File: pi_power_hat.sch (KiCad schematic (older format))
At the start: 21 parts, among them J1 GPIO_CONNECTOR, J2 Barrel_Jack, J3 PIR Motion Sensor, J4 DH22T, J5 Screw_Terminal_01x02, Q1 DMG1012UW-7

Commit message: Add input connectors
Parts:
- J2: footprint (none) -> CON-SOCJ-2155:GRAVITECH_CON-SOCJ-2155; symbol Connector:Barrel_Jack -> Connector:Barrel_Jack_Switch
- J5: footprint (none) -> CONN-TH_P5.00_KF301-5.0-2P:CONN-TH_P5.00_KF301-5.0-2P
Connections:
- net IN-: now also J2.3
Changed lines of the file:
@@
 F 0 "J5" H 1780 942 50  0000 L CNN
 F 1 "Screw_Terminal_01x02" H 1780 851 50  0000 L CNN
-F 2 "" H 1700 950 50  0001 C CNN
-F 3 "~" H 1700 950 50  0001 C CNN
+F 2 "CONN-TH_P5.00_KF301-5.0-2P:CONN-TH_P5.00_KF301-5.0-2P" H 1700 950 50  0001 C CNN
+F 3 "https://www.lcsc.com/product-detail/Screw-terminal_Cixi-Kefa-Elec-KF301-5-0-2P_C474881.html" H 1700 950 50  0001 C CNN
 	1    1700 950
 	-1   0    0    -1
 $EndComp
 $Comp
-L Connector:Barrel_Jack J2
+L Connector:Barrel_Jack_Switch J2
 U 1 1 61C4808D
 P 1650 1550
 F 0 "J2" H 1707 1875 50  0000 C CNN
 F 1 "Barrel_Jack" H 1707 1784 50  0000 C CNN
-F 2 "" H 1700 1510 50  0001 C CNN
-F 3 "~" H 1700 1510 50  0001 C CNN
+F 2 "CON-SOCJ-2155:GRAVITECH_CON-SOCJ-2155" H 1700 1510 50  0001 C CNN
+F 3 "~https://www.mouser.be/ProductDetail/Gravitech/CON-SOCJ-2155?qs=fkzBJ5HM%252BdCcpvFQyQZHtA%3D%3D" H 1700 1510 50  0001 C CNN
 	1    1650 1550
 	1    0    0    -1
@@
 IN-
 Wire Wire Line
-	1950 1650 2300 1650
+	1950 1650 2050 1650
 Text Label 2300 1650 2    50   ~ 0
 IN-
@@
 	1    0    0    -1
 $EndComp
+Wire Wire Line
+	1950 1550 2050 1550
+Wire Wire Line
+	2050 1550 2050 1650
+Connection ~ 2050 1650
+Wire Wire Line
+	2050 1650 2300 1650
 $EndSCHEMATC

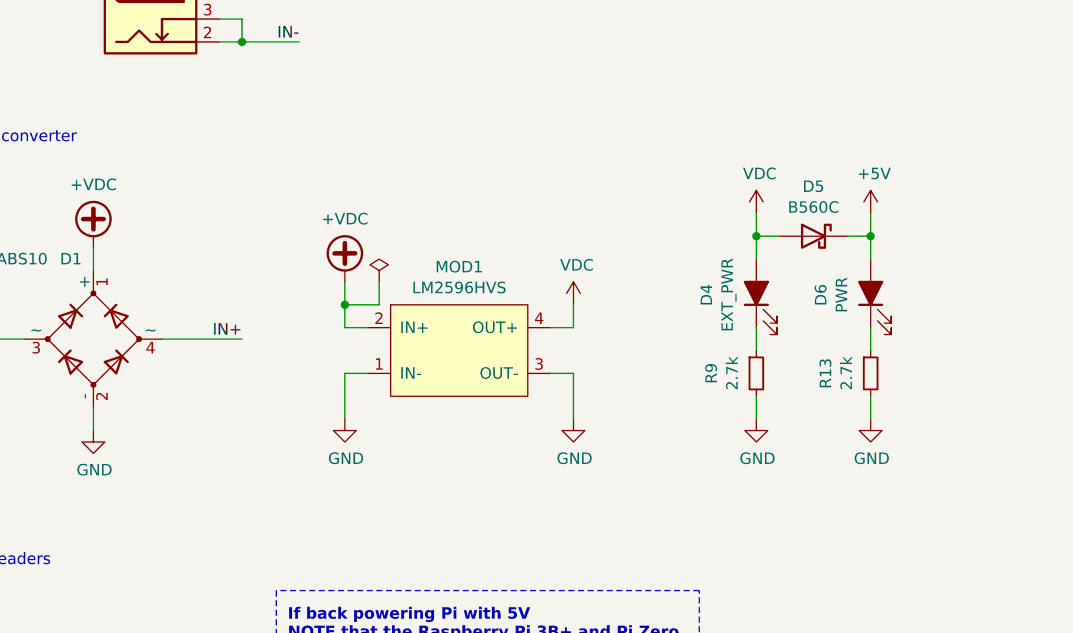
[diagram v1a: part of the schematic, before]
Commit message: Add fuse
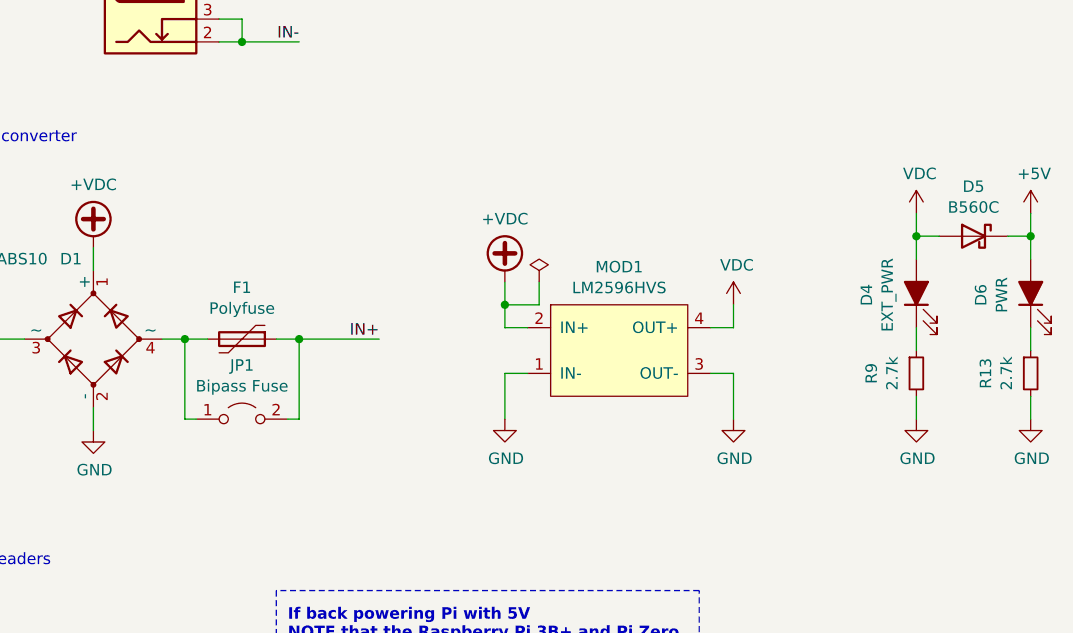
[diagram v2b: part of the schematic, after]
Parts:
- added F1: Polyfuse, FUSE-TH_L10.4-W3.1-P5.10-D0.8-S1.50:FUSE-TH_L10.4-W3.1-P5.10-D0.8-S1.50, symbol Device:Polyfuse
- added JP1: Bipass Fuse, Jumper:SolderJumper-2_P1.3mm_Open_RoundedPad1.0x1.5mm, symbol Jumper:Jumper_2_Open
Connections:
- net IN+: now also F1.1, JP1.2 (B); no longer D1.4 (~~)
- new net: D1.4 (~~), F1.2, JP1.1 (A)
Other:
- moved on the sheet: D4, D5, D6, MOD1, R13, R9
